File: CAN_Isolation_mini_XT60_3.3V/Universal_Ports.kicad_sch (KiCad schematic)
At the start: 21 parts, among them J10 Conn_01x04_Pin, J11 Conn_01x04_Pin, J12 Conn_01x04_Pin, J13 Conn_01x04_Pin, J14 Conn_01x04_Pin, J15 Conn_01x04_Pin, J16 Conn_01x04_Pin, J17 Conn_01x04_Pin, J18 S2B-XH-A, J19 S2B-XH-A, J2 Conn_01x04_Pin, J20 S5B-XH-A, J21 XT60PW-F, J22 XT60PW-F, J3 Conn_01x04_Pin, J4 Conn_01x04_Pin, J5 Conn_01x04_Pin, J6 Conn_01x04_Pin, J7 Conn_01x04_Pin, J8 Conn_01x04_Pin, J9 Conn_01x04_Pin

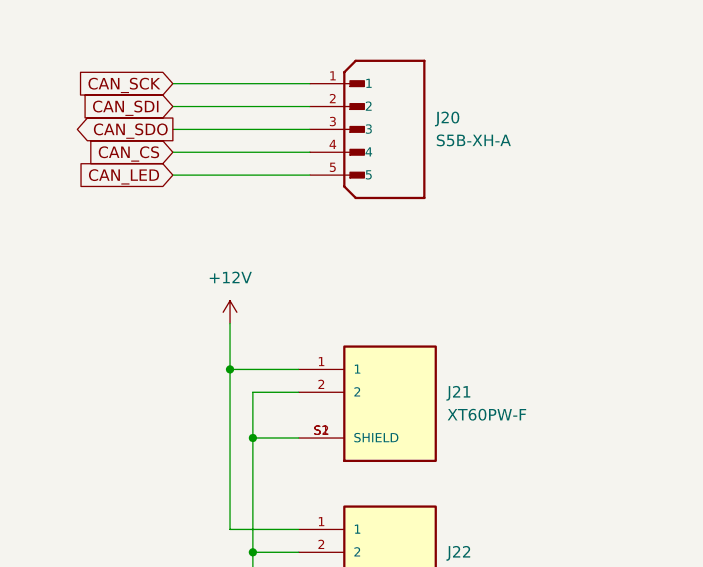
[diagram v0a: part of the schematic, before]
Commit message: Add diode for servo line.
Add diode for servo line.
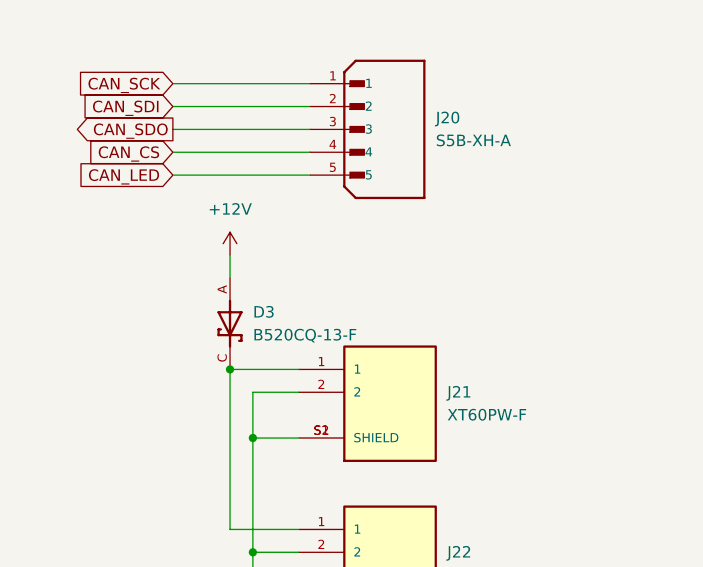
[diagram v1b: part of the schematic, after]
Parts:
- added D3: B520CQ-13-F, CAN_Isolation:DIOM7959X250N, symbol B520CQ-13-F:B520CQ-13-F
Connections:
- net +12V: now also D3.A; no longer J21.1, J22.1
- new net: D3.C, J21.1, J22.1
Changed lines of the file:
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@@
+	)
+	(junction
+		(at 54.61 144.78)
+		(diameter 0)
+		(color 0 0 0 0)
 	)
 	(junction
@@
 	)
 	(junction
-		(at 54.61 144.78)
-		(diameter 0)
-		(color 0 0 0 0)
-	)
-	(junction
 		(at 127 31.75)
 		(diameter 0)
@@
 	(wire
 		(pts
-			(xy 54.61 144.78) (xy 54.61 139.7)
-		)
-		(stroke
-			(width 0)
-			(type default)
-		)
-	)
-	(wire
-		(pts
 			(xy 60.96 48.26) (xy 60.96 50.8)
 		)
@@
 		(pts
 			(xy 57.15 165.1) (xy 62.23 165.1)
+		)
+		(stroke
+			(width 0)
+			(type default)
+		)
+	)
+	(wire
+		(pts
+			(xy 54.61 132.08) (xy 54.61 134.62)
 		)
 		(stroke
@@
 	(symbol
 		(lib_id "power:+12V")
-		(at 54.61 139.7 0)
+		(at 54.61 132.08 0)
 		(unit 1)
 		(exclude_from_sim no)
@@
 		(fields_autoplaced yes)
 		(property "Reference" "#PWR031"
-			(at 54.61 143.51 0)
+			(at 54.61 135.89 0)
 			(effects
 				(font
@@
 		)
 		(property "Value" "+12V"
-			(at 54.61 134.62 0)
+			(at 54.61 127 0)
 			(effects
 				(font
@@
 		)
 		(property "Footprint" ""
-			(at 54.61 139.7 0)
+			(at 54.61 132.08 0)
 			(effects
 				(font
@@
 		)
 		(property "Datasheet" ""
-			(at 54.61 139.7 0)
+			(at 54.61 132.08 0)
 			(effects
 				(font
@@
 		)
 		(property "Description" "Power symbol creates a global label with name \"+12V\""
-			(at 54.61 139.7 0)
+			(at 54.61 132.08 0)
 			(effects
 				(font
@@
 					(unit 1)
 				)
+			)
+		)
+	)
+	(symbol
+		(lib_id "B520CQ-13-F:B520CQ-13-F")
+		(at 54.61 139.7 270)
+		(unit 1)
+		(exclude_from_sim no)
+		(in_bom yes)
+		(on_board yes)
+		(dnp no)
+		(fields_autoplaced yes)
+		(property "Reference" "D3"
+			(at 57.15 138.4299 90)
+			(effects
+				(font
+					(size 1.27 1.27)
+				)
+				(justify left)
+			)
+		)
+		(property "Value" "B520CQ-13-F"
+			(at 57.15 140.9699 90)
+			(effects
+				(font
+					(size 1.27 1.27)
+				)
+				(justify left)
+			)
+		)
+		(property "Footprint" "CAN_Isolation:DIOM7959X250N"
+			(at 54.61 139.7 0)
+			(effects
+				(font
+					(size 1.27 1.27)
+				)
+				(justify bottom)
+				(hide yes)
+			)
+		)
+		(property "Datasheet" ""
+			(at 54.61 139.7 0)
+			(effects
+				(font
+					(size 1.27 1.27)
+				)
+				(hide yes)
+			)
+		)
+		(property "Description" ""
+			(at 54.61 139.7 0)
+			(effects
+				(font
+					(size 1.27 1.27)
+				)
+				(hide yes)
+			)
+		)
+		(property "MANUFACTURER" "Diodes Inc"
+			(at 54.61 139.7 0)
+			(effects
+				(font
+					(size 1.27 1.27)
+				)
+				(justify bottom)
+				(hide yes)
+			)
+		)
+		(pin "A"
+		)
+		(pin "C"
+		)
+		(instances
+			(project ""
+				(path "/d188d587-a283-4d42-bf18-6e85dcc02a49/54dda61f-9174-4ddd-af5e-6bc53d2182b0"
+					(reference "D3")
+					(unit 1)
+				)

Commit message: Fix XT60 line.
Fix XT60 line.
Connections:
- net +12V: now also J22.1
- net at D3.C, J21.1: no longer J22.1
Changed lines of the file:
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@@
-	)
-	(junction
-		(at 54.61 144.78)
-		(diameter 0)
-		(color 0 0 0 0)
 	)
 	(junction
@@
 	)
 	(junction
+		(at 54.61 133.35)
+		(diameter 0)
+		(color 0 0 0 0)
+	)
+	(junction
 		(at 60.96 50.8)
 		(diameter 0)
@@
 	(wire
 		(pts
+			(xy 46.99 162.56) (xy 46.99 133.35)
+		)
+		(stroke
+			(width 0)
+			(type default)
+		)
+	)
+	(wire
+		(pts
+			(xy 46.99 133.35) (xy 54.61 133.35)
+		)
+		(stroke
+			(width 0)
+			(type default)
+		)
+	)
+	(wire
+		(pts
+			(xy 46.99 162.56) (xy 62.23 162.56)
+		)
+		(stroke
+			(width 0)
+			(type default)
+		)
+	)
+	(wire
+		(pts
 			(xy 127 50.8) (xy 127 53.34)
 		)
@@
 	(wire
 		(pts
-			(xy 54.61 132.08) (xy 54.61 134.62)
+			(xy 54.61 132.08) (xy 54.61 133.35)
 		)
 		(stroke
@@
 	(wire
 		(pts
+			(xy 54.61 133.35) (xy 54.61 134.62)
+		)
+		(stroke
+			(width 0)
+			(type default)
+		)
+	)
+	(wire
+		(pts
 			(xy 127 29.21) (xy 127 31.75)
 		)
@@
 	(wire
 		(pts
-			(xy 62.23 162.56) (xy 54.61 162.56)
-		)
-		(stroke
-			(width 0)
-			(type default)
-		)
-	)
-	(wire
-		(pts
 			(xy 58.42 91.44) (xy 62.23 91.44)
 		)
@@
 		)
 		(stroke
-			(width 0)
-			(type default)
-		)
-	)
-	(wire
-		(pts
-			(xy 54.61 162.56) (xy 54.61 144.78)
-		)
-		(stroke
